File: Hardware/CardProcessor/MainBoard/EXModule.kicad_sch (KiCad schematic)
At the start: 0 parts

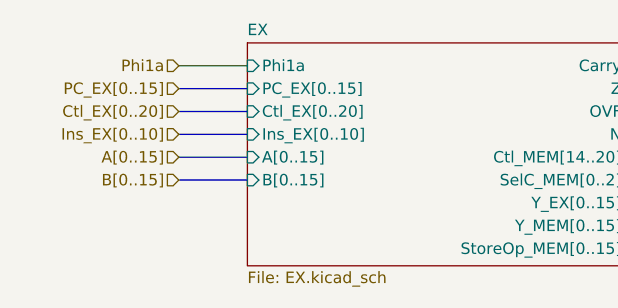
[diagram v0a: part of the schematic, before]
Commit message: Split net Phi1a into Phi1a and Phi1e
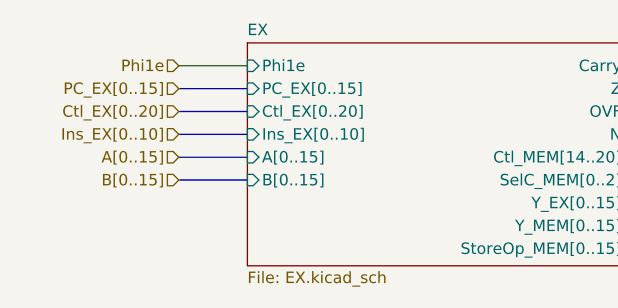
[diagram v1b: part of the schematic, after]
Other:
- sheet EX ports: added Phi1e; removed Phi1a
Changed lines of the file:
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@@
 		)
 	)
-	(hierarchical_label "Phi1a"
+	(hierarchical_label "Phi1e"
 		(shape input)
 		(at 110.49 80.01 180)
@@
 			)
 		)
-		(pin "Phi1a" input
+		(pin "Phi1e" input
 			(at 118.11 80.01 180)
 			(effects

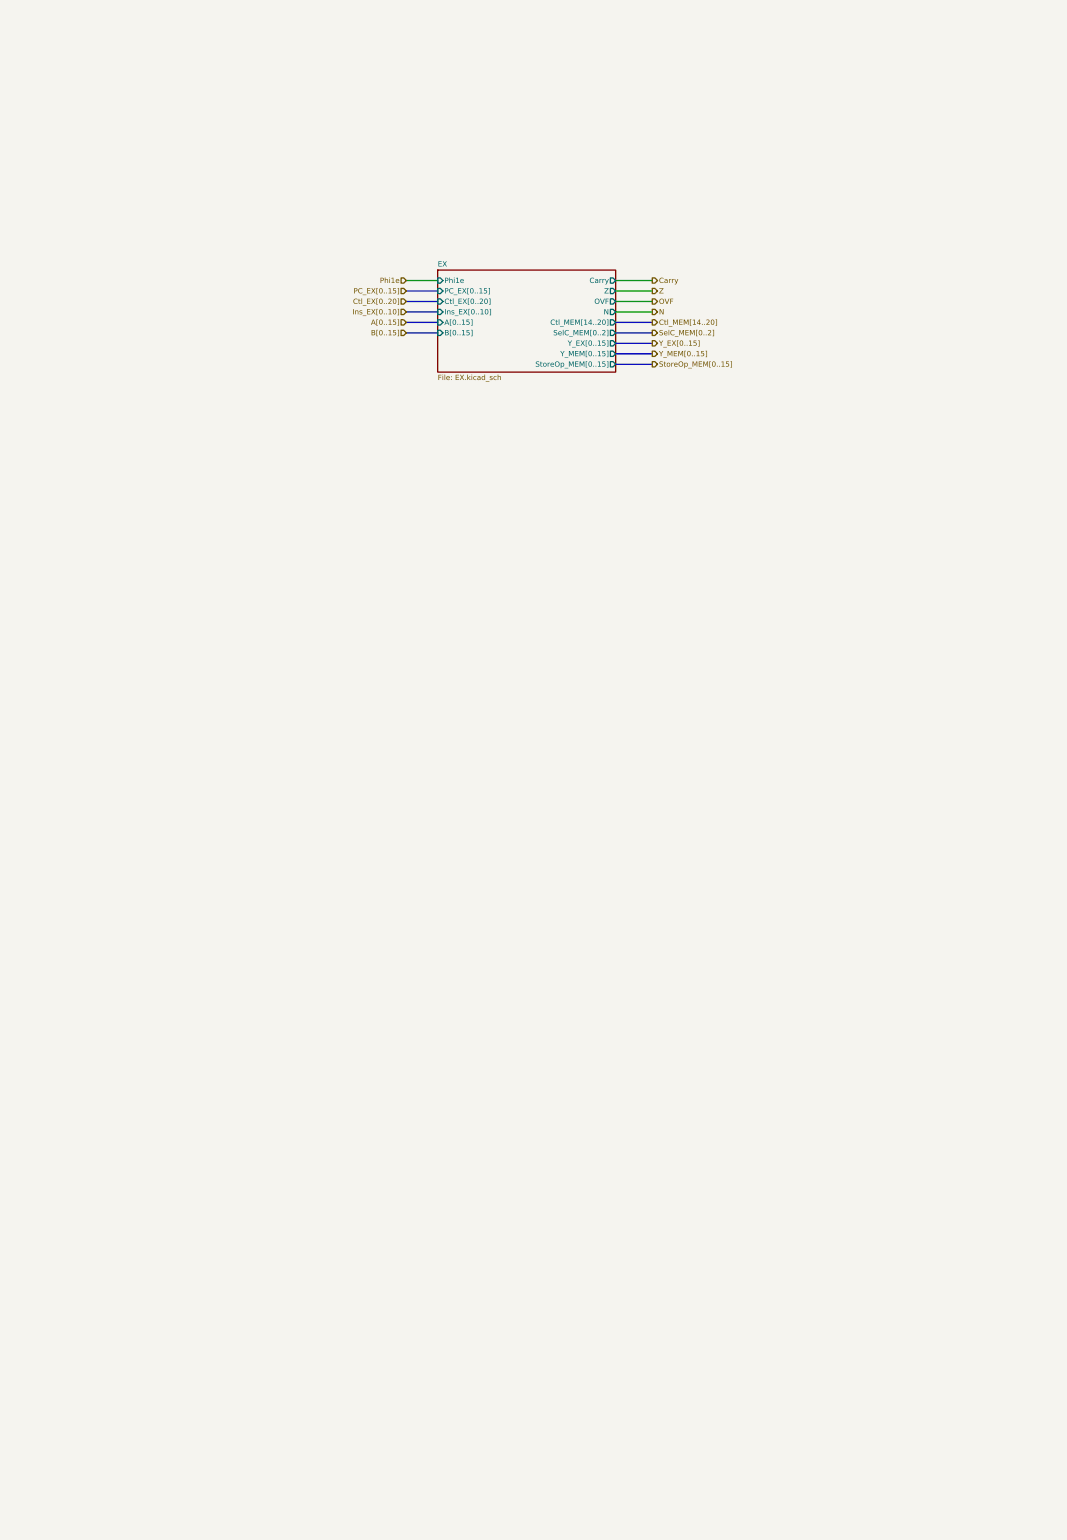
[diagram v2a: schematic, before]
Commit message: Replace EXModule with a connector to a separate PCB
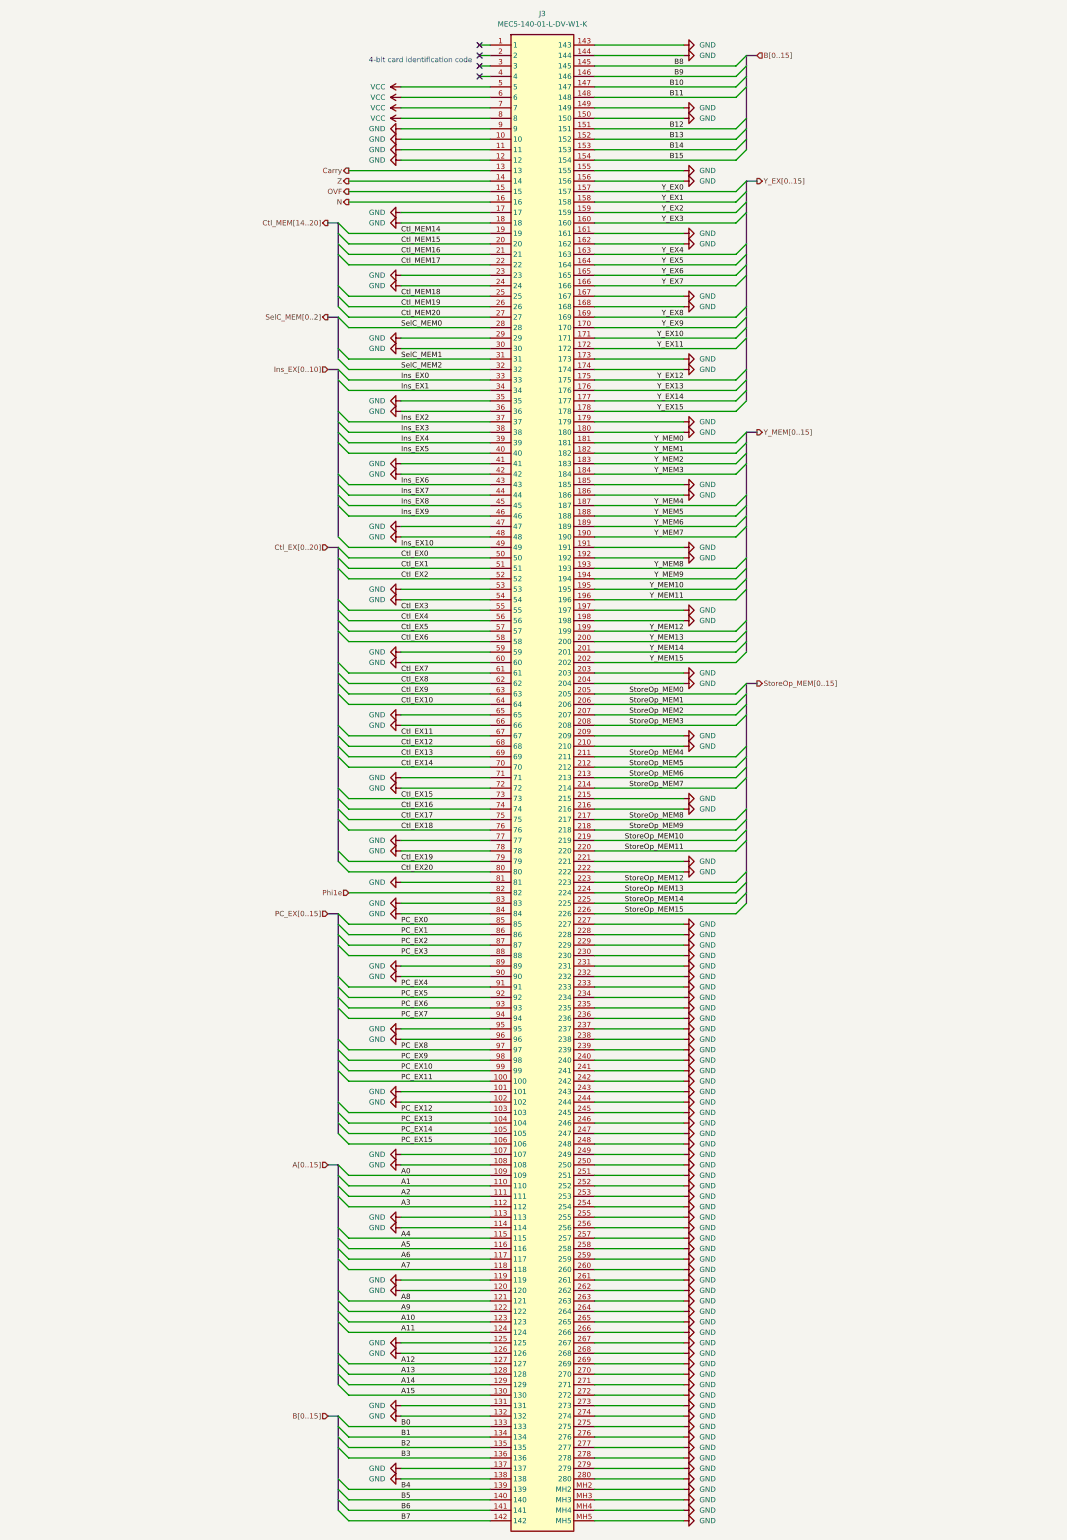
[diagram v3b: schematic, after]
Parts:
- added J3: MEC5-140-01-L-DV-W1-K, Turtle16:MEC514001LDVW1K, symbol Turtle16:MEC5-140-01-L-DV-W1-K
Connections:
- net Carry: now also J3.13
- net N: now also J3.16
- net OVF: now also J3.15
- net Phi1e: now also J3.82
- net Z: now also J3.14
- new net A0: J3.109
- new net A1: J3.110
- new net A10: J3.123
- new net A11: J3.124
- new net A12: J3.127
- new net A13: J3.128
- new net A14: J3.129
- new net A15: J3.130
- new net A2: J3.111
- new net A3: J3.112
- new net A4: J3.115
- new net A5: J3.116
- new net A6: J3.117
- new net A7: J3.118
- new net A8: J3.121
- new net A9: J3.122
- new net B0: J3.133
- new net B1: J3.134
- new net B10: J3.147
- new net B11: J3.148
- new net B12: J3.151
- new net B13: J3.152
- new net B14: J3.153
- new net B15: J3.154
- new net B2: J3.135
- new net B3: J3.136
- new net B4: J3.139
- new net B5: J3.140
- new net B6: J3.141
- new net B7: J3.142
- new net B8: J3.145
- new net B9: J3.146
- new net Ctl_EX0: J3.50
- new net Ctl_EX1: J3.51
- new net Ctl_EX10: J3.64
- new net Ctl_EX11: J3.67
- new net Ctl_EX12: J3.68
- new net Ctl_EX13: J3.69
- new net Ctl_EX14: J3.70
- new net Ctl_EX15: J3.73
- new net Ctl_EX16: J3.74
- new net Ctl_EX17: J3.75
- new net Ctl_EX18: J3.76
- new net Ctl_EX19: J3.79
- new net Ctl_EX2: J3.52
- new net Ctl_EX20: J3.80
- new net Ctl_EX3: J3.55
- new net Ctl_EX4: J3.56
- new net Ctl_EX5: J3.57
- new net Ctl_EX6: J3.58
- new net Ctl_EX7: J3.61
- new net Ctl_EX8: J3.62
- new net Ctl_EX9: J3.63
- new net Ctl_MEM14: J3.19
- new net Ctl_MEM15: J3.20
- new net Ctl_MEM16: J3.21
- new net Ctl_MEM17: J3.22
- new net Ctl_MEM18: J3.25
- new net Ctl_MEM19: J3.26
- new net Ctl_MEM20: J3.27
- new net GND: J3.10, J3.101, J3.102, J3.107, J3.108, J3.11, J3.113, J3.114, J3.119, J3.12, J3.120, J3.125, J3.126, J3.131, J3.132, J3.137, J3.138, J3.143, J3.144, J3.149, J3.150, J3.155, J3.156, J3.161, J3.162, J3.167, J3.168, J3.17, J3.173, J3.174, J3.179, J3.18, J3.180, J3.185, J3.186, J3.191, J3.192, J3.197, J3.198, J3.203, J3.204, J3.209, J3.210, J3.215, J3.216, J3.221, J3.222, J3.227, J3.228, J3.229, J3.23, J3.230, J3.231, J3.232, J3.233, J3.234, J3.235, J3.236, J3.237, J3.238, J3.239, J3.24, J3.240, J3.241, J3.242, J3.243, J3.244, J3.245, J3.246, J3.247, J3.248, J3.249, J3.250, J3.251, J3.252, J3.253, J3.254, J3.255, J3.256, J3.257, J3.258, J3.259, J3.260, J3.261, J3.262, J3.263, J3.264, J3.265, J3.266, J3.267, J3.268, J3.269, J3.270, J3.271, J3.272, J3.273, J3.274, J3.275, J3.276, J3.277, J3.278, J3.279, J3.280, J3.29, J3.30, J3.35, J3.36, J3.41, J3.42, J3.47, J3.48, J3.53, J3.54, J3.59, J3.60, J3.65, J3.66, J3.71, J3.72, J3.77, J3.78, J3.81, J3.83, J3.84, J3.89, J3.9, J3.90, J3.95, J3.96, J3.MH2, J3.MH3, J3.MH4, J3.MH5
- new net Ins_EX0: J3.33
- new net Ins_EX1: J3.34
- new net Ins_EX10: J3.49
- new net Ins_EX2: J3.37
- new net Ins_EX3: J3.38
- new net Ins_EX4: J3.39
- new net Ins_EX5: J3.40
- new net Ins_EX6: J3.43
- new net Ins_EX7: J3.44
- new net Ins_EX8: J3.45
- new net Ins_EX9: J3.46
- new net PC_EX0: J3.85
- new net PC_EX1: J3.86
- new net PC_EX10: J3.99
- new net PC_EX11: J3.100
- new net PC_EX12: J3.103
- new net PC_EX13: J3.104
- new net PC_EX14: J3.105
- new net PC_EX15: J3.106
- new net PC_EX2: J3.87
- new net PC_EX3: J3.88
- new net PC_EX4: J3.91
- new net PC_EX5: J3.92
- new net PC_EX6: J3.93
- new net PC_EX7: J3.94
- new net PC_EX8: J3.97
- new net PC_EX9: J3.98
- new net SelC_MEM0: J3.28
- new net SelC_MEM1: J3.31
- new net SelC_MEM2: J3.32
- new net StoreOp_MEM0: J3.205
- new net StoreOp_MEM1: J3.206
- new net StoreOp_MEM10: J3.219
- new net StoreOp_MEM11: J3.220
- new net StoreOp_MEM12: J3.223
- new net StoreOp_MEM13: J3.224
- new net StoreOp_MEM14: J3.225
- new net StoreOp_MEM15: J3.226
- new net StoreOp_MEM2: J3.207
- new net StoreOp_MEM3: J3.208
- new net StoreOp_MEM4: J3.211
- new net StoreOp_MEM5: J3.212
- new net StoreOp_MEM6: J3.213
- new net StoreOp_MEM7: J3.214
- new net StoreOp_MEM8: J3.217
- new net StoreOp_MEM9: J3.218
- new net VCC: J3.5, J3.6, J3.7, J3.8
- new net Y_EX0: J3.157
- new net Y_EX1: J3.158
- new net Y_EX10: J3.171
- new net Y_EX11: J3.172
- new net Y_EX12: J3.175
- new net Y_EX13: J3.176
- new net Y_EX14: J3.177
- new net Y_EX15: J3.178
- new net Y_EX2: J3.159
- new net Y_EX3: J3.160
- new net Y_EX4: J3.163
- new net Y_EX5: J3.164
- new net Y_EX6: J3.165
- new net Y_EX7: J3.166
- new net Y_EX8: J3.169
- new net Y_EX9: J3.170
- new net Y_MEM0: J3.181
- new net Y_MEM1: J3.182
- new net Y_MEM10: J3.195
- new net Y_MEM11: J3.196
- new net Y_MEM12: J3.199
- new net Y_MEM13: J3.200
- new net Y_MEM14: J3.201
- new net Y_MEM15: J3.202
- new net Y_MEM2: J3.183
- new net Y_MEM3: J3.184
- new net Y_MEM4: J3.187
- new net Y_MEM5: J3.188
- new net Y_MEM6: J3.189
- new net Y_MEM7: J3.190
- new net Y_MEM8: J3.193
- new net Y_MEM9: J3.194
- no-connect marks 0 -> 4
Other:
- removed sheet EX
- note added: "4-bit card identification code"
